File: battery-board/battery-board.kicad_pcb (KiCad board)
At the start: 2 copper layers, 57.5 x 29 mm, 1 part

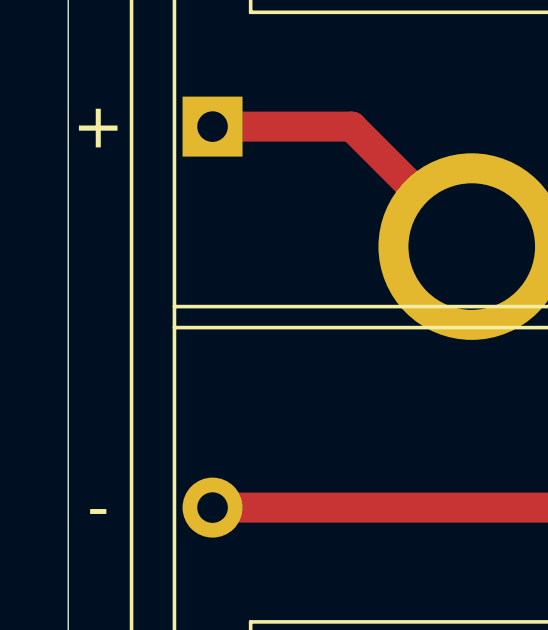
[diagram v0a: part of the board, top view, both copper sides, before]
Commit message: Added version number to boards.
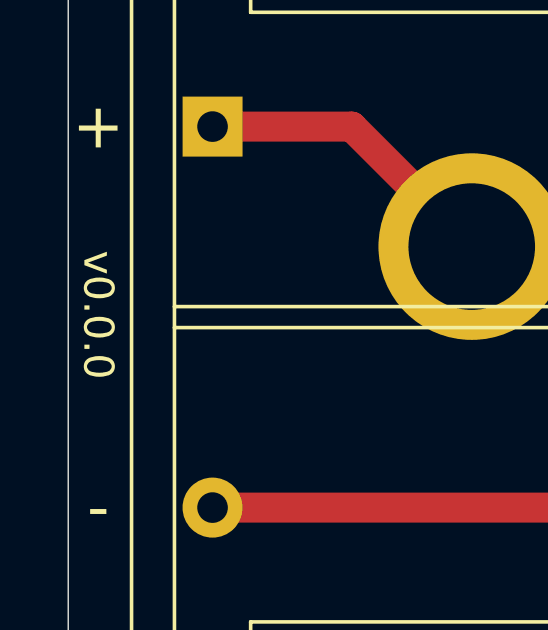
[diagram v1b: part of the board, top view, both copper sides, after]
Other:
- board text added: "v0.0.0"
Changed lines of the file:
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@@
   (general
     (thickness 1.6)
-    (drawings 8)
+    (drawings 9)
     (tracks 5)
     (zones 0)
@@
       (effects (font (size 1 1) (thickness 0.15)))
     )
+    (fp_line (start 50.89 19.15) (end 50.89 -6.45) (layer F.CrtYd) (width 0.05))
+    (fp_line (start -3.09 19.15) (end 50.89 19.15) (layer F.CrtYd) (width 0.05))
+    (fp_line (start -3.09 -6.45) (end -3.09 19.15) (layer F.CrtYd) (width 0.05))
+    (fp_line (start 50.89 -6.45) (end -3.09 -6.45) (layer F.CrtYd) (width 0.05))
+    (fp_line (start 50.5 18.75) (end 50.5 -6.05) (layer F.SilkS) (width 0.12))
+    (fp_line (start -2.7 18.755) (end 50.5 18.755) (layer F.SilkS) (width 0.12))
+    (fp_line (start -2.7 -6.05) (end -2.7 18.75) (layer F.SilkS) (width 0.12))
+    (fp_line (start 50.5 -6.055) (end -2.7 -6.055) (layer F.SilkS) (width 0.12))
+    (fp_line (start 13.97 15.24) (end 13.97 10.16) (layer F.SilkS) (width 0.12))
+    (fp_line (start 13.97 10.16) (end 32.56 10.16) (layer F.SilkS) (width 0.12))
+    (fp_line (start 32.56 10.16) (end 32.56 11.43) (layer F.SilkS) (width 0.12))
+    (fp_line (start 32.56 11.43) (end 33.83 11.43) (layer F.SilkS) (width 0.12))
+    (fp_line (start 33.83 11.43) (end 33.83 13.97) (layer F.SilkS) (width 0.12))
+    (fp_line (start 33.83 13.97) (end 32.56 13.97) (layer F.SilkS) (width 0.12))
+    (fp_line (start 32.56 13.97) (end 32.56 15.24) (layer F.SilkS) (width 0.12))
+    (fp_line (start 32.56 15.24) (end 13.97 15.24) (layer F.SilkS) (width 0.12))
+    (fp_line (start 33.83 2.54) (end 15.24 2.54) (layer F.SilkS) (width 0.12))
+    (fp_line (start 15.24 2.54) (end 15.24 1.27) (layer F.SilkS) (width 0.12))
+    (fp_line (start 15.24 1.27) (end 13.97 1.27) (layer F.SilkS) (width 0.12))
+    (fp_line (start 13.97 1.27) (end 13.97 -1.27) (layer F.SilkS) (width 0.12))
+    (fp_line (start 13.97 -1.27) (end 15.24 -1.27) (layer F.SilkS) (width 0.12))
+    (fp_line (start 15.24 -1.27) (end 15.24 -2.54) (layer F.SilkS) (width 0.12))
+    (fp_line (start 15.24 -2.54) (end 33.83 -2.54) (layer F.SilkS) (width 0.12))
+    (fp_line (start 33.83 -2.54) (end 33.83 2.54) (layer F.SilkS) (width 0.12))
+    (fp_line (start -1.27 6) (end 21.59 6) (layer F.SilkS) (width 0.12))
+    (fp_line (start 21.59 6) (end 21.59 6.7) (layer F.SilkS) (width 0.12))
+    (fp_line (start 21.59 6.7) (end -1.27 6.7) (layer F.SilkS) (width 0.12))
+    (fp_line (start 49.07 6) (end 28.75 6) (layer F.SilkS) (width 0.12))
+    (fp_line (start 28.75 6) (end 28.75 6.7) (layer F.SilkS) (width 0.12))
+    (fp_line (start 28.75 6.7) (end 49.07 6.7) (layer F.SilkS) (width 0.12))
+    (fp_line (start 13.97 16.51) (end 13.97 17.78) (layer F.SilkS) (width 0.12))
+    (fp_line (start 13.97 17.78) (end 33.83 17.78) (layer F.SilkS) (width 0.12))
+    (fp_line (start 33.83 17.78) (end 33.83 16.51) (layer F.SilkS) (width 0.12))
+    (fp_line (start 46.53 -3.81) (end 33.83 -3.81) (layer F.SilkS) (width 0.12))
+    (fp_line (start 33.83 -3.81) (end 33.83 -5.08) (layer F.SilkS) (width 0.12))
+    (fp_line (start 33.83 -5.08) (end 13.97 -5.08) (layer F.SilkS) (width 0.12))
+    (fp_line (start 13.97 -5.08) (end 13.97 -3.81) (layer F.SilkS) (width 0.12))
+    (fp_line (start 46.53 16.51) (end 33.83 16.51) (layer F.SilkS) (width 0.12))
+    (fp_line (start 1.27 -3.81) (end 13.97 -3.81) (layer F.SilkS) (width 0.12))
+    (fp_line (start 1.27 -3.81) (end 1.27 -5.08) (layer F.SilkS) (width 0.12))
+    (fp_line (start 1.27 -5.08) (end -1.27 -5.08) (layer F.SilkS) (width 0.12))
+    (fp_line (start -1.27 -5.08) (end -1.27 17.78) (layer F.SilkS) (width 0.12))
+    (fp_line (start -1.27 17.78) (end 1.27 17.78) (layer F.SilkS) (width 0.12))
+    (fp_line (start 1.27 17.78) (end 1.27 16.51) (layer F.SilkS) (width 0.12))
+    (fp_line (start 1.27 16.51) (end 13.97 16.51) (layer F.SilkS) (width 0.12))
+    (fp_line (start 49.07 -5.08) (end 46.53 -5.08) (layer F.SilkS) (width 0.12))
+    (fp_line (start 46.53 -5.08) (end 46.53 -3.81) (layer F.SilkS) (width 0.12))
+    (fp_line (start 49.07 -5.08) (end 49.07 17.78) (layer F.SilkS) (width 0.12))
+    (fp_line (start 49.07 17.78) (end 46.53 17.78) (layer F.SilkS) (width 0.12))
+    (fp_line (start 46.53 17.78) (end 46.53 16.51) (layer F.SilkS) (width 0.12))
+    (fp_line (start -2.59 18.645) (end -2.59 -5.945) (layer F.Fab) (width 0.1))
+    (fp_line (start 50.39 18.645) (end 50.39 -5.945) (layer F.Fab) (width 0.1))
+    (fp_line (start -2.59 18.645) (end 50.39 18.645) (layer F.Fab) (width 0.1))
     (fp_line (start -2.59 -5.945) (end 50.39 -5.945) (layer F.Fab) (width 0.1))
-    (fp_line (start -2.59 18.645) (end 50.39 18.645) (layer F.Fab) (width 0.1))
-    (fp_line (start 50.39 18.645) (end 50.39 -5.945) (layer F.Fab) (width 0.1))
-    (fp_line (start -2.59 18.645) (end -2.59 -5.945) (layer F.Fab) (width 0.1))
-    (fp_line (start 46.53 17.78) (end 46.53 16.51) (layer F.SilkS) (width 0.12))
-    (fp_line (start 49.07 17.78) (end 46.53 17.78) (layer F.SilkS) (width 0.12))
-    (fp_line (start 49.07 -5.08) (end 49.07 17.78) (layer F.SilkS) (width 0.12))
-    (fp_line (start 46.53 -5.08) (end 46.53 -3.81) (layer F.SilkS) (width 0.12))
-    (fp_line (start 49.07 -5.08) (end 46.53 -5.08) (layer F.SilkS) (width 0.12))
-    (fp_line (start 1.27 16.51) (end 13.97 16.51) (layer F.SilkS) (width 0.12))
-    (fp_line (start 1.27 17.78) (end 1.27 16.51) (layer F.SilkS) (width 0.12))
-    (fp_line (start -1.27 17.78) (end 1.27 17.78) (layer F.SilkS) (width 0.12))
-    (fp_line (start -1.27 -5.08) (end -1.27 17.78) (layer F.SilkS) (width 0.12))
-    (fp_line (start 1.27 -5.08) (end -1.27 -5.08) (layer F.SilkS) (width 0.12))
-    (fp_line (start 1.27 -3.81) (end 1.27 -5.08) (layer F.SilkS) (width 0.12))
-    (fp_line (start 1.27 -3.81) (end 13.97 -3.81) (layer F.SilkS) (width 0.12))
-    (fp_line (start 46.53 16.51) (end 33.83 16.51) (layer F.SilkS) (width 0.12))
-    (fp_line (start 13.97 -5.08) (end 13.97 -3.81) (layer F.SilkS) (width 0.12))
-    (fp_line (start 33.83 -5.08) (end 13.97 -5.08) (layer F.SilkS) (width 0.12))
-    (fp_line (start 33.83 -3.81) (end 33.83 -5.08) (layer F.SilkS) (width 0.12))
-    (fp_line (start 46.53 -3.81) (end 33.83 -3.81) (layer F.SilkS) (width 0.12))
-    (fp_line (start 33.83 17.78) (end 33.83 16.51) (layer F.SilkS) (width 0.12))
-    (fp_line (start 13.97 17.78) (end 33.83 17.78) (layer F.SilkS) (width 0.12))
-    (fp_line (start 13.97 16.51) (end 13.97 17.78) (layer F.SilkS) (width 0.12))
-    (fp_line (start 28.75 6.7) (end 49.07 6.7) (layer F.SilkS) (width 0.12))
-    (fp_line (start 28.75 6) (end 28.75 6.7) (layer F.SilkS) (width 0.12))
-    (fp_line (start 49.07 6) (end 28.75 6) (layer F.SilkS) (width 0.12))
-    (fp_line (start 21.59 6.7) (end -1.27 6.7) (layer F.SilkS) (width 0.12))
-    (fp_line (start 21.59 6) (end 21.59 6.7) (layer F.SilkS) (width 0.12))
-    (fp_line (start -1.27 6) (end 21.59 6) (layer F.SilkS) (width 0.12))
-    (fp_line (start 33.83 -2.54) (end 33.83 2.54) (layer F.SilkS) (width 0.12))
-    (fp_line (start 15.24 -2.54) (end 33.83 -2.54) (layer F.SilkS) (width 0.12))
-    (fp_line (start 15.24 -1.27) (end 15.24 -2.54) (layer F.SilkS) (width 0.12))
-    (fp_line (start 13.97 -1.27) (end 15.24 -1.27) (layer F.SilkS) (width 0.12))
-    (fp_line (start 13.97 1.27) (end 13.97 -1.27) (layer F.SilkS) (width 0.12))
-    (fp_line (start 15.24 1.27) (end 13.97 1.27) (layer F.SilkS) (width 0.12))
-    (fp_line (start 15.24 2.54) (end 15.24 1.27) (layer F.SilkS) (width 0.12))
-    (fp_line (start 33.83 2.54) (end 15.24 2.54) (layer F.SilkS) (width 0.12))
-    (fp_line (start 32.56 15.24) (end 13.97 15.24) (layer F.SilkS) (width 0.12))
-    (fp_line (start 32.56 13.97) (end 32.56 15.24) (layer F.SilkS) (width 0.12))
-    (fp_line (start 33.83 13.97) (end 32.56 13.97) (layer F.SilkS) (width 0.12))
-    (fp_line (start 33.83 11.43) (end 33.83 13.97) (layer F.SilkS) (width 0.12))
-    (fp_line (start 32.56 11.43) (end 33.83 11.43) (layer F.SilkS) (width 0.12))
-    (fp_line (start 32.56 10.16) (end 32.56 11.43) (layer F.SilkS) (width 0.12))
-    (fp_line (start 13.97 10.16) (end 32.56 10.16) (layer F.SilkS) (width 0.12))
-    (fp_line (start 13.97 15.24) (end 13.97 10.16) (layer F.SilkS) (width 0.12))
-    (fp_line (start 50.5 -6.055) (end -2.7 -6.055) (layer F.SilkS) (width 0.12))
-    (fp_line (start -2.7 -6.05) (end -2.7 18.75) (layer F.SilkS) (width 0.12))
-    (fp_line (start -2.7 18.755) (end 50.5 18.755) (layer F.SilkS) (width 0.12))
-    (fp_line (start 50.5 18.75) (end 50.5 -6.05) (layer F.SilkS) (width 0.12))
-    (fp_line (start 50.89 -6.45) (end -3.09 -6.45) (layer F.CrtYd) (width 0.05))
-    (fp_line (start -3.09 -6.45) (end -3.09 19.15) (layer F.CrtYd) (width 0.05))
-    (fp_line (start -3.09 19.15) (end 50.89 19.15) (layer F.CrtYd) (width 0.05))
-    (fp_line (start 50.89 19.15) (end 50.89 -6.45) (layer F.CrtYd) (width 0.05))
     (fp_text user + (at 35.1 12.7) (layer F.SilkS)
       (effects (font (size 1.5 1.5) (thickness 0.15)))
@@
     )
   )
+  (gr_text v0.0.0 (at 1 14.4 270) (layer F.SilkS)
+    (effects (font (size 1 1) (thickness 0.15)))
+  )
   (gr_arc (start 55 26.5) (end 55 29) (angle -90) (layer Edge.Cuts) (width 0.05))
